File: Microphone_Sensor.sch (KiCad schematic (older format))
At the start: 31 parts, among them J4 Mic_Conn, U4 MAX4063

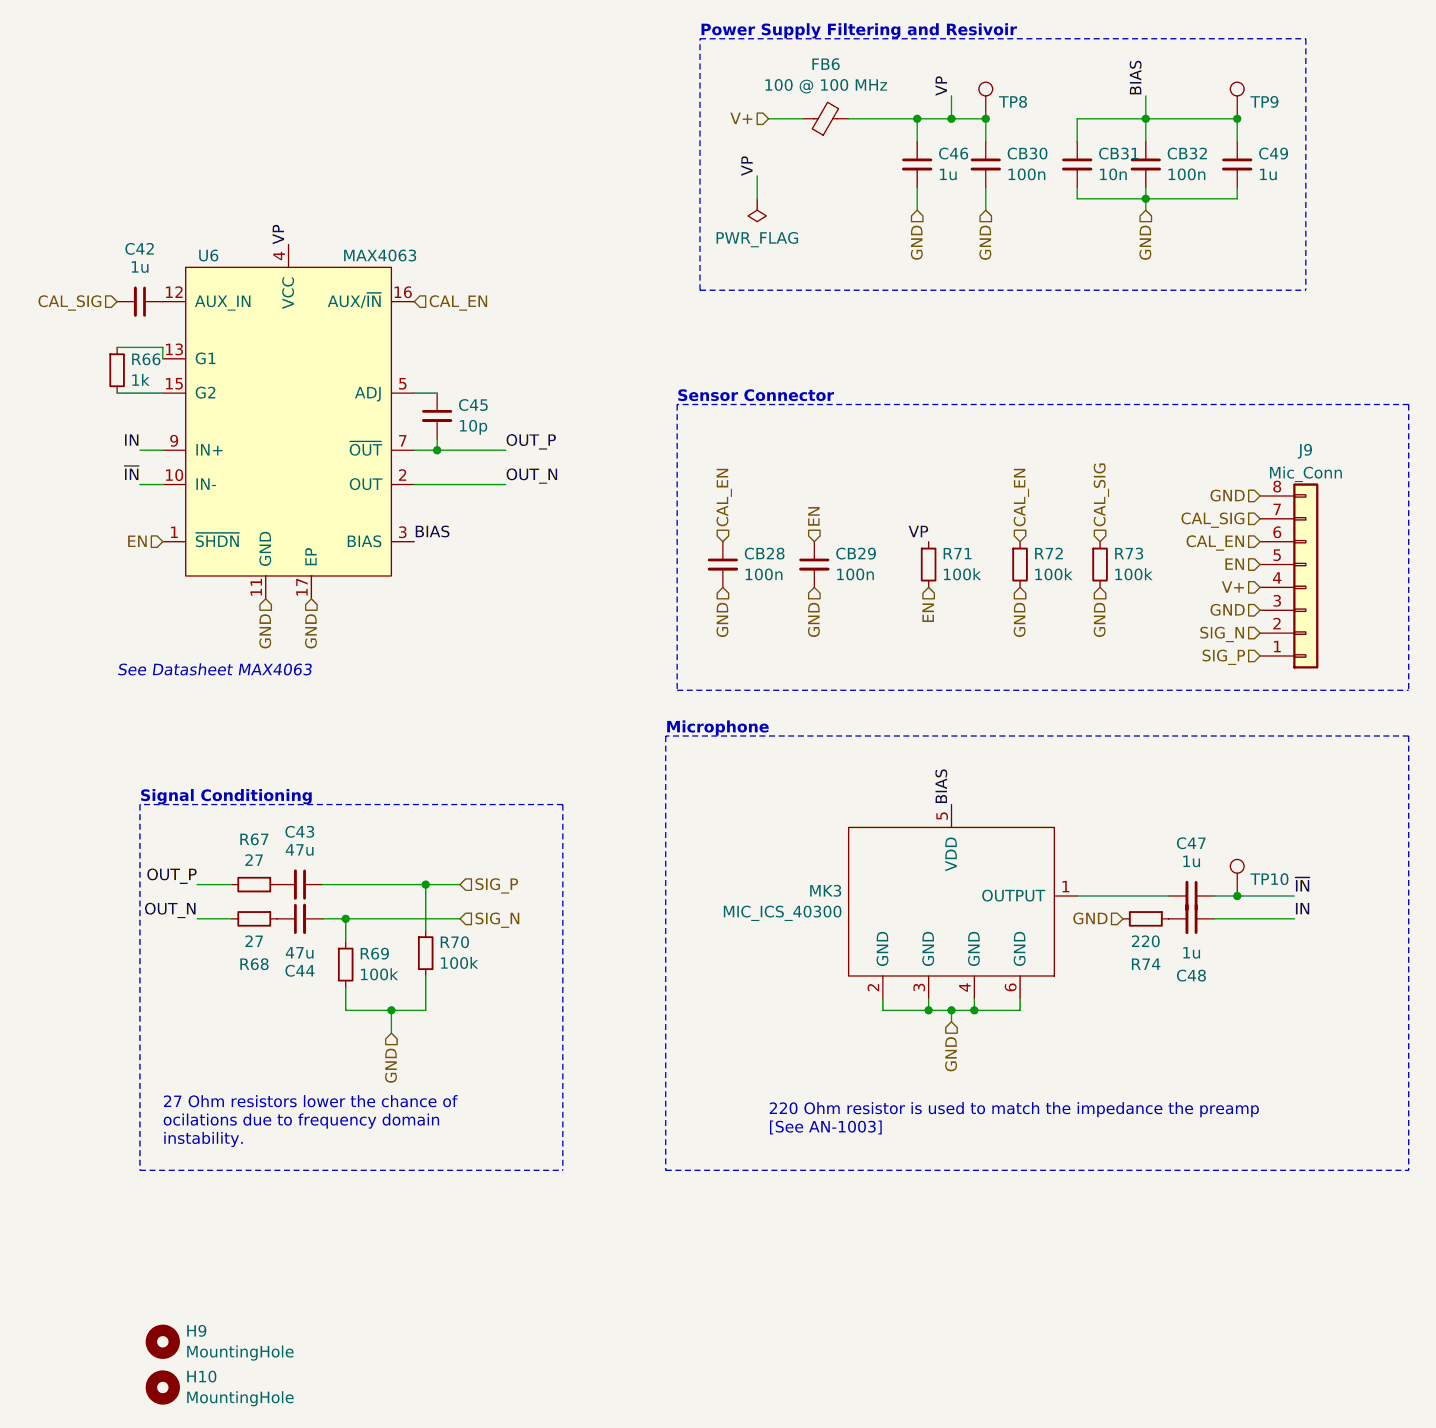
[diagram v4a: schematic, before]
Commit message: CHange to single 3 designs to save cost
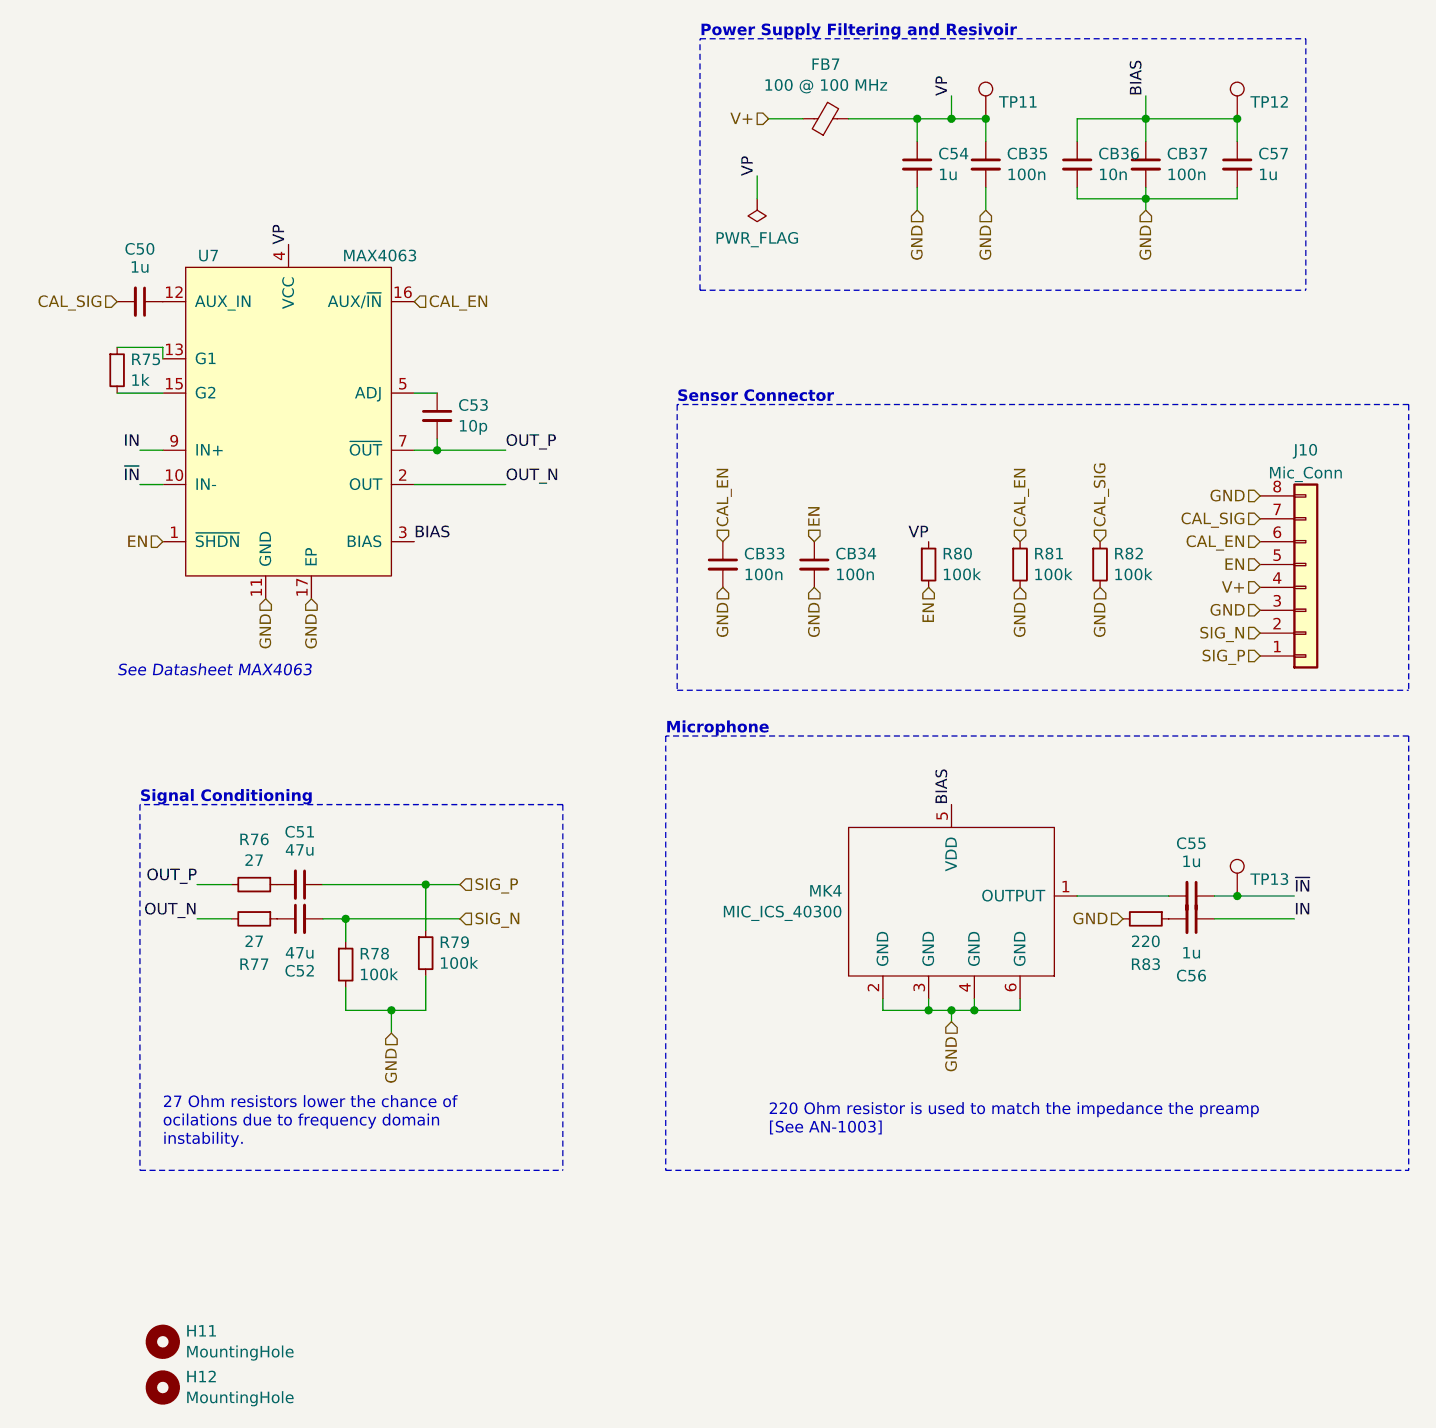
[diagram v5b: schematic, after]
